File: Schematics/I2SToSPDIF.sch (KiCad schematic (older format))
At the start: 9 parts, among them Q3 2N7000, U3 WM8804, Y1 12Mhz

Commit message: Fixed CDC interface schematic; Fixed SPDIF output interface schematic; Added screw terminals; Modified PCB design
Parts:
- Q3: footprint Package_TO_SOT_THT:TO-92_Inline -> Package_TO_SOT_THT:TO-92_Inline_Wide
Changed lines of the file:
@@
 F 0 "Q3" H 3800 2950 50  0000 L CNN
 F 1 "2N7000" H 3800 2850 50  0000 L CNN
-F 2 "Package_TO_SOT_THT:TO-92_Inline" H 3800 2725 50  0001 L CIN
+F 2 "Package_TO_SOT_THT:TO-92_Inline_Wide" H 3800 2725 50  0001 L CIN
 F 3 "https://www.fairchildsemi.com/datasheets/2N/2N7000.pdf" H 3600 2800 50  0001 L CNN
 	1    3600 2800

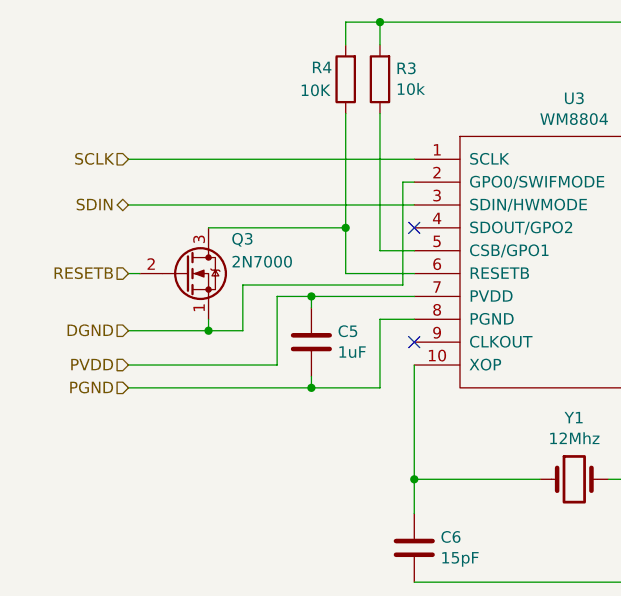
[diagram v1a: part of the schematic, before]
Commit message: Added R28 to Q3 between pin 1 and 2; Updated PCB design
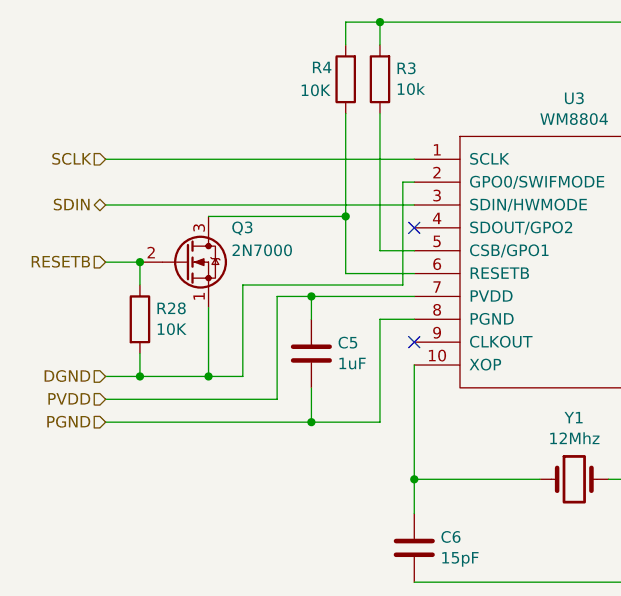
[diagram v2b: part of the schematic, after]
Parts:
- added R28: 10K, Resistor_THT:R_Axial_DIN0204_L3.6mm_D1.6mm_P2.54mm_Vertical, symbol Device:R
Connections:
- net DGND: now also R28.2
- net RESETB: now also R28.1
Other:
- moved on the sheet: C5, Q3
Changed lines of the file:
@@
 $EndDescr
 Wire Wire Line
-	4150 3300 4450 3300
-Wire Wire Line
-	4150 3250 4150 3300
-Wire Wire Line
-	4150 2950 4150 2900
+	4150 3450 4450 3450
+Wire Wire Line
+	4150 3300 4150 3450
+Wire Wire Line
+	4150 3000 4150 2900
 Wire Wire Line
 	6500 2100 6500 2150
@@
 	6150 2400 6150 2100
 Wire Wire Line
-	4450 3000 4450 3300
+	4450 3000 4450 3450
 Wire Wire Line
 	4600 3000 4450 3000
@@
 L Device:C C?
 U 1 1 5CCA1ADD
-P 4150 3100
+P 4150 3150
 AR Path="/5CCA1ADD" Ref="C?"  Part="1"
 AR Path="/5CCA0E0E/5CCA1ADD" Ref="C5"  Part="1"
-F 0 "C5" H 4265 3146 50  0000 L CNN
-F 1 "1uF" H 4265 3055 50  0000 L CNN
-F 2 "Capacitor_THT:C_Rect_L7.2mm_W5.5mm_P5.00mm_FKS2_FKP2_MKS2_MKP2" H 4188 2950 50  0001 C CNN
-F 3 "~" H 4150 3100 50  0001 C CNN
-	1    4150 3100
+F 0 "C5" H 4265 3196 50  0000 L CNN
+F 1 "1uF" H 4265 3105 50  0000 L CNN
+F 2 "Capacitor_THT:C_Rect_L7.2mm_W5.5mm_P5.00mm_FKS2_FKP2_MKS2_MKP2" H 4188 3000 50  0001 C CNN
+F 3 "~" H 4150 3150 50  0001 C CNN
+	1    4150 3150
 	1    0    0    -1
 $EndComp
@@
 Text HLabel 7050 2100 2    50   Input ~ 0
 DVDD
-Text HLabel 3350 3200 0    50   Input ~ 0
+Text HLabel 3250 3350 0    50   Input ~ 0
 PVDD
-Text HLabel 3350 3300 0    50   Input ~ 0
+Text HLabel 3250 3450 0    50   Input ~ 0
 PGND
 Text HLabel 7050 2500 2    50   Input ~ 0
@@
 Wire Wire Line
 	4150 2900 4600 2900
-Connection ~ 4150 3300
+Connection ~ 4150 3450
 Connection ~ 6500 2500
 Wire Wire Line
@@
 	6000 2500 6150 2500
 Connection ~ 6150 2500
-Text HLabel 3350 2300 0    50   Input ~ 0
+Text HLabel 3250 2300 0    50   Input ~ 0
 SCLK
-Text HLabel 3350 2500 0    50   BiDi ~ 0
+Text HLabel 3250 2500 0    50   BiDi ~ 0
 SDIN
-Text HLabel 3350 2800 0    50   Input ~ 0
+Text HLabel 3250 2750 0    50   Input ~ 0
 RESETB
 Connection ~ 6850 2500
@@
 L Transistor_FET:2N7000 Q3
 U 1 1 5D0A1A0C
-P 3600 2800
-F 0 "Q3" H 3800 2950 50  0000 L CNN
-F 1 "2N7000" H 3800 2850 50  0000 L CNN
-F 2 "Package_TO_SOT_THT:TO-92_Inline_Wide" H 3800 2725 50  0001 L CIN
-F 3 "https://www.fairchildsemi.com/datasheets/2N/2N7000.pdf" H 3600 2800 50  0001 L CNN
-	1    3600 2800
+P 3600 2750
+F 0 "Q3" H 3800 2900 50  0000 L CNN
+F 1 "2N7000" H 3800 2800 50  0000 L CNN
+F 2 "Package_TO_SOT_THT:TO-92_Inline_Wide" H 3800 2675 50  0001 L CIN
+F 3 "https://www.fairchildsemi.com/datasheets/2N/2N7000.pdf" H 3600 2750 50  0001 L CNN
+	1    3600 2750
 	1    0    0    -1
 $EndComp
@@
 	4300 1700 4450 1700
 Wire Wire Line
-	3350 3200 4000 3200
-Wire Wire Line
-	4000 3200 4000 2900
+	3250 3350 4000 3350
+Wire Wire Line
+	4000 3350 4000 2900
 Wire Wire Line
 	4000 2900 4150 2900
@@
 	4600 2400 4550 2400
 Wire Wire Line
-	4300 2100 4300 2600
+	4300 2100 4300 2550
 Wire Wire Line
 	4300 2800 4600 2800
 Wire Wire Line
-	3350 3300 4150 3300
-Text HLabel 3350 3050 0    50   Input ~ 0
+	3250 3450 4150 3450
+Text HLabel 3250 3250 0    50   Input ~ 0
 DGND
 Wire Wire Line
-	3700 2600 4300 2600
-Connection ~ 4300 2600
-Wire Wire Line
-	4300 2600 4300 2800
-Wire Wire Line
-	3350 3050 3700 3050
-Wire Wire Line
-	3700 3050 3700 3000
-Wire Wire Line
-	3350 2800 3400 2800
-Wire Wire Line
-	3700 3050 3850 3050
-Wire Wire Line
-	3850 3050 3850 2850
+	3700 2550 4300 2550
+Connection ~ 4300 2550
+Wire Wire Line
+	4300 2550 4300 2800
+Wire Wire Line
+	3250 3250 3400 3250
+Wire Wire Line
+	3700 3250 3700 2950
+Wire Wire Line
+	3250 2750 3400 2750
+Wire Wire Line
+	3700 3250 3850 3250
+Wire Wire Line
+	3850 3250 3850 2850
 Wire Wire Line
 	3850 2850 4550 2850
 Wire Wire Line
 	4550 2850 4550 2400
-Connection ~ 3700 3050
-Wire Wire Line
-	3350 2500 4600 2500
-Wire Wire Line
-	3350 2300 4600 2300
+Connection ~ 3700 3250
+Wire Wire Line
+	3250 2500 4600 2500
+Wire Wire Line
+	3250 2300 4600 2300
+$Comp
+L Device:R R28
+U 1 1 5D51D75E
+P 3400 3000
+F 0 "R28" H 3470 3046 50  0000 L CNN
+F 1 "10K" H 3470 2955 50  0000 L CNN
+F 2 "Resistor_THT:R_Axial_DIN0204_L3.6mm_D1.6mm_P2.54mm_Vertical" V 3330 3000 50  0001 C CNN
+F 3 "~" H 3400 3000 50  0001 C CNN
+	1    3400 3000
+	1    0    0    -1
+$EndComp
+Wire Wire Line
+	3400 3150 3400 3250
+Connection ~ 3400 3250
+Wire Wire Line
+	3400 3250 3700 3250
+Wire Wire Line
+	3400 2850 3400 2750
+Connection ~ 3400 2750
 $EndSCHEMATC
